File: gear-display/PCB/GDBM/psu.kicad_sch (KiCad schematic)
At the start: 10 parts

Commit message: new features
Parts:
- added C? (x2): C_1206_10u_50V, KD_Capacitor:C_1206_3216Metric, symbol KD_Capacitor:C_1206_10u_50V
- added C?: C_0603_100n_X7R_100V, KD_Capacitor:C_0603_1608Metric, symbol KD_Capacitor:C_0603_100n_X7R_100V
- added U?: DC_DC_5V_0A5_K78U05-500R3, KD_IC_DCDC_Converter:DC_DC_Mornsun_K78U05-500R3_H, symbol KD_IC_Regulator_DC_Converter:DC_DC_5V_0A5_K78U05-500R3
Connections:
- net +12V: now also U?.1 (VI)
- net GND: now also C?.2, C?.2, C?.2, U?.2 (GND)
- new net +5V: C?.1, C?.1, C?.1, U?.3 (VO)
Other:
- moved on the sheet: C?, D?, F?, J?, U?

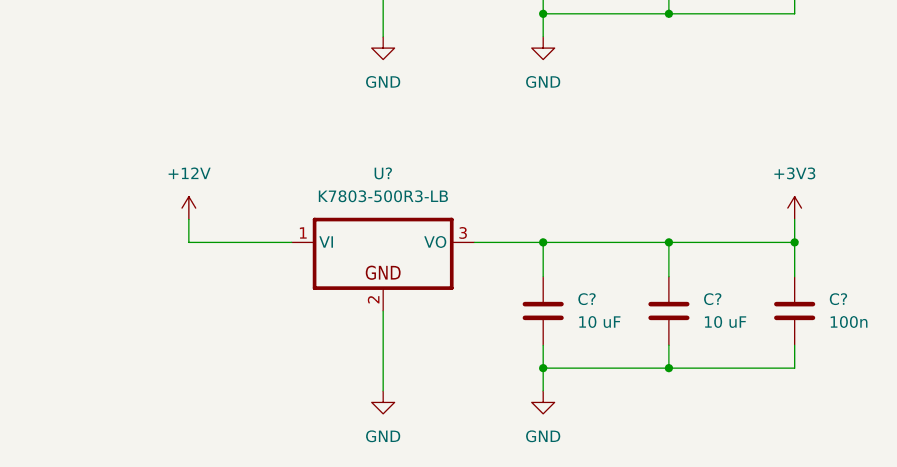
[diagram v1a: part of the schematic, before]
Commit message: changed to match simhub conf
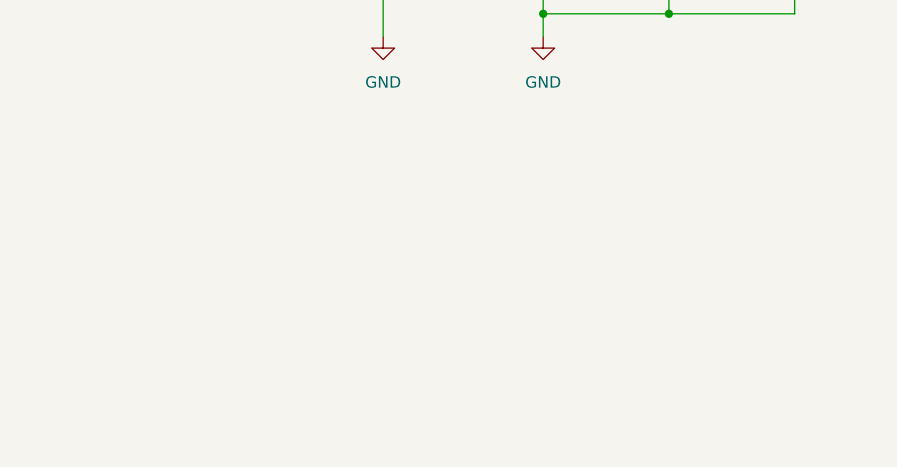
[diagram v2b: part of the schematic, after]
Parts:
- removed C?: C_0603_100n_X7R_100V, KD_Capacitor:C_0603_1608Metric, symbol KD_Capacitor:C_0603_100n_X7R_100V
- removed C? (x2): C_1206_10u_50V, KD_Capacitor:C_1206_3216Metric, symbol KD_Capacitor:C_1206_10u_50V
- removed U?: DC_DC_3V3+-_0A5_K7803-500R3-LB, KD_IC_DCDC_Converter:DC_DC_Mornsun_K78xx-500R3-LB, symbol KD_IC_Regulator_DC_Converter:DC_DC_3V3+-_0A5_K7803-500R3-LB

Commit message: rikki
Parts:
- removed D?: TVS_36V_SMAJ36CA, KD_Diode:D_SMA, symbol KD_Diode:TVS_36V_SMAJ36CA
- added D2: TVS_12V_LF_SMAJ12CA, KD_Diode:DIOC530X280X230_SMA_A, symbol KD_Diode:TVS_12V_LF_SMAJ12CA
- F1: renamed from F?; footprint KD_Resistor:R_1206_3216Metric -> KD_Resistor:RESC3216X70N
- gave numbers to parts that had none: 8
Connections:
- net +12V: now also D2.1 (K)
- net GND renamed Earth
- net Earth: now also D2.2 (A)
- no-connect marks 0 -> 1
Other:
- note removed: "SMAJ16 or something?"

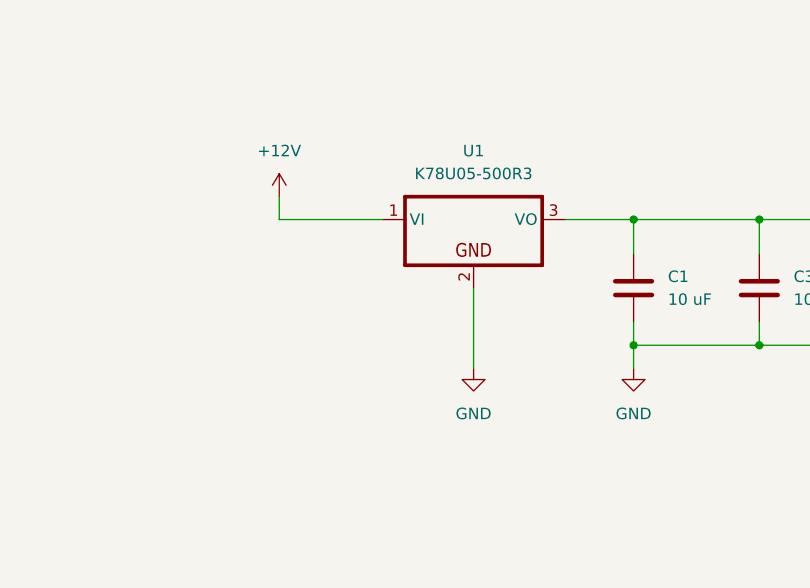
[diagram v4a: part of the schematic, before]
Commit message: PSU and LED powering changed
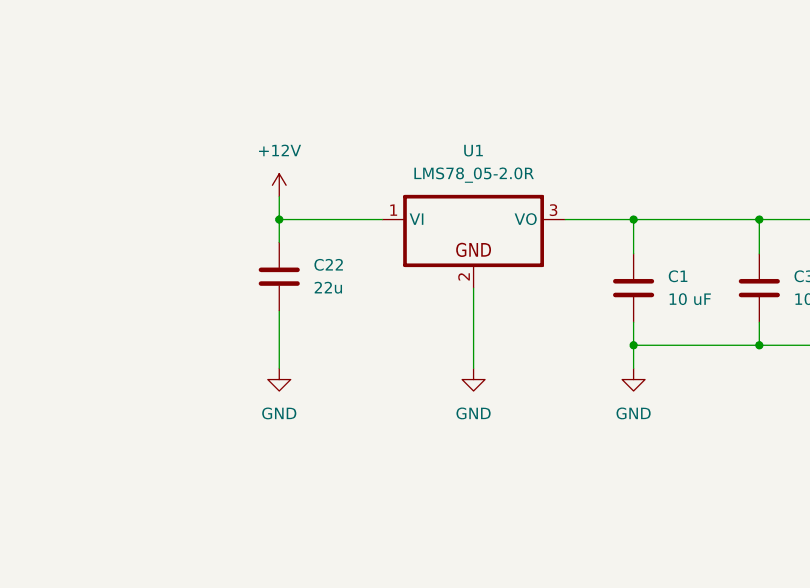
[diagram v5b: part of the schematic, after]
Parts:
- added C22: C_0805_22u_X5R_10V, KD_Capacitor:CAPC2012X135N, symbol KD_Capacitor:C_0805_22u_X5R_10V
- C1, C2, C3: footprint KD_Capacitor:C_1206_3216Metric -> KD_Capacitor:CAPC3216X150N
- C4, C5: footprint KD_Capacitor:C_0603_1608Metric -> KD_Capacitor:CAPC1608X90N
- U1: footprint KD_IC_DCDC_Converter:DC_DC_Mornsun_K78U05-500R3_H -> KD_IC_DCDC_Converter:DC_DC_GAPTEC_OKI-78SR-5_H; symbol KD_IC_Regulator_DC_Converter:DC_DC_5V_0A5_K78U05-500R3 -> KD_IC_Regulator_DC_Converter:DC_DC_5V_2A0_GAPTEC_OKI-78SR-5_H; Code K78U05-500R3 -> LMS78_05-2.0R; MFG_PartNo K78U05-500R3 -> LMS78_05-2.0R; Manufacturer Mornsun America, LLC -> GAPTEC Electronic; Price 3 -> 5; Supplier_PartNo 2725-K78U05-500R3-ND -> 3182-LMS78_05-2.0R-ND
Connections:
- net +12V: now also C22.1
- net Earth: now also C22.2
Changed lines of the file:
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@@
   (junction (at 181.61 111.76) (diameter 0) (color 0 0 0 0)
+  )
+  (junction (at 128.27 97.79) (diameter 0) (color 0 0 0 0)
   )
   (junction (at 167.64 97.79) (diameter 0) (color 0 0 0 0)
@@
     (stroke (width 0) (type default) (color 0 0 0 0))
   )
+  (wire (pts (xy 128.27 114.3) (xy 128.27 107.95))
+    (stroke (width 0) (type default) (color 0 0 0 0))
+  )
   (wire (pts (xy 104.14 149.86) (xy 104.14 147.32))
     (stroke (width 0) (type default) (color 0 0 0 0))
@@
     (stroke (width 0) (type default) (color 0 0 0 0))
   )
+  (wire (pts (xy 128.27 97.79) (xy 128.27 100.33))
+    (stroke (width 0) (type default) (color 0 0 0 0))
+  )
   (wire (pts (xy 181.61 109.22) (xy 181.61 111.76))
     (stroke (width 0) (type default) (color 0 0 0 0))
@@
       (effects (font (size 1.27 1.27)) (justify left) hide)
     )
-    (property "Footprint" "KD_Capacitor:C_0603_1608Metric" (id 2) (at 182.88 40.64 0)
+    (property "Footprint" "KD_Capacitor:CAPC1608X90N" (id 2) (at 182.88 40.64 0)
       (effects (font (size 1.27 1.27)) (justify left) hide)
     )
@@
     (pin "2")
   )
-  (symbol (lib_id "KD_IC_Regulator_DC_Converter:DC_DC_5V_0A5_K78U05-500R3") (at 149.86 97.79 0) (unit 1)
+  (symbol (lib_id "KD_IC_Regulator_DC_Converter:DC_DC_5V_2A0_GAPTEC_OKI-78SR-5_H") (at 149.86 97.79 0) (unit 1)
     (in_bom yes) (on_board yes) (fields_autoplaced)
     (property "Reference" "U1" (id 0) (at 149.86 90.17 0))
@@
       (effects (font (size 1.27 1.27)) (justify left) hide)
     )
-    (property "Footprint" "KD_IC_DCDC_Converter:DC_DC_Mornsun_K78U05-500R3_H" (id 2) (at 137.16 83.82 0)
-      (effects (font (size 1.27 1.27)) (justify left) hide)
-    )
-    (property "Datasheet" "https://www.mornsun-power.com/html/pdf/K78U05-500R3.html" (id 3) (at 137.16 86.36 0)
-      (effects (font (size 1.27 1.27)) (justify left) hide)
-    )
-    (property "Code" "K78U05-500R3" (id 4) (at 149.86 92.71 0))
-    (property "Manufacturer" "Mornsun America, LLC" (id 5) (at 137.16 68.58 0)
-      (effects (font (size 1.27 1.27)) (justify left) hide)
-    )
-    (property "MFG_PartNo" "K78U05-500R3" (id 6) (at 137.16 71.12 0)
+    (property "Footprint" "KD_IC_DCDC_Converter:DC_DC_GAPTEC_OKI-78SR-5_H" (id 2) (at 137.16 83.82 0)
+      (effects (font (size 1.27 1.27)) (justify left) hide)
+    )
+    (property "Datasheet" "https://gaptec-electronic.com/datenblaetter/LMS78_2.0R.pdf" (id 3) (at 137.16 86.36 0)
+      (effects (font (size 1.27 1.27)) (justify left) hide)
+    )
+    (property "Code" "LMS78_05-2.0R" (id 4) (at 149.86 92.71 0))
+    (property "Manufacturer" "GAPTEC Electronic" (id 5) (at 137.16 68.58 0)
+      (effects (font (size 1.27 1.27)) (justify left) hide)
+    )
+    (property "MFG_PartNo" "LMS78_05-2.0R" (id 6) (at 137.16 71.12 0)
       (effects (font (size 1.27 1.27)) (justify left) hide)
     )
@@
       (effects (font (size 1.27 1.27)) (justify left) hide)
     )
-    (property "Supplier_PartNo" "2725-K78U05-500R3-ND" (id 8) (at 137.16 76.2 0)
+    (property "Supplier_PartNo" "3182-LMS78_05-2.0R-ND" (id 8) (at 137.16 76.2 0)
       (effects (font (size 1.27 1.27)) (justify left) hide)
     )
@@
       (effects (font (size 1.27 1.27)) (justify left) hide)
     )
-    (property "Price" "3" (id 10) (at 137.16 81.28 0)
+    (property "Price" "5" (id 10) (at 137.16 81.28 0)
       (effects (font (size 1.27 1.27)) (justify left) hide)
     )
@@
     (pin "3")
   )
-  (symbol (lib_id "KD_Capacitor:C_1206_10u_50V") (at 167.64 105.41 0) (unit 1)
+  (symbol (lib_name "C_1206_10u_50V_1") (lib_id "KD_Capacitor:C_1206_10u_50V") (at 167.64 105.41 0) (unit 1)
     (in_bom yes) (on_board yes) (fields_autoplaced)
     (property "Reference" "C1" (id 0) (at 171.45 104.1399 0)
@@
       (effects (font (size 1.27 1.27)) (justify left) hide)
     )
-    (property "Footprint" "KD_Capacitor:C_1206_3216Metric" (id 2) (at 154.94 91.44 0)
+    (property "Footprint" "KD_Capacitor:CAPC3216X150N" (id 2) (at 154.94 91.44 0)
       (effects (font (size 1.27 1.27)) (justify left) hide)
     )
@@
       (effects (font (size 1.27 1.27)) (justify left) hide)
     )
-    (property "Footprint" "KD_Capacitor:C_1206_3216Metric" (id 2) (at 165.1 40.64 0)
+    (property "Footprint" "KD_Capacitor:CAPC3216X150N" (id 2) (at 165.1 40.64 0)
       (effects (font (size 1.27 1.27)) (justify left) hide)
     )
@@
     (pin "1")
   )
-  (symbol (lib_id "KD_Capacitor:C_0603_100n_X7R_100V") (at 195.58 105.41 0) (unit 1)
+  (symbol (lib_name "C_0603_100n_X7R_100V_1") (lib_id "KD_Capacitor:C_0603_100n_X7R_100V") (at 195.58 105.41 0) (unit 1)
     (in_bom yes) (on_board yes) (fields_autoplaced)
     (property "Reference" "C5" (id 0) (at 199.39 104.1399 0)
@@
       (effects (font (size 1.27 1.27)) (justify left) hide)
     )
-    (property "Footprint" "KD_Capacitor:C_0603_1608Metric" (id 2) (at 182.88 91.44 0)
+    (property "Footprint" "KD_Capacitor:CAPC1608X90N" (id 2) (at 182.88 91.44 0)
       (effects (font (size 1.27 1.27)) (justify left) hide)
     )
@@
     (pin "1")
     (pin "2")
+  )
+  (symbol (lib_id "power:GND") (at 128.27 114.3 0) (unit 1)
+    (in_bom yes) (on_board yes) (fields_autoplaced)
+    (property "Reference" "#PWR0145" (id 0) (at 128.27 120.65 0)
+      (effects (font (size 1.27 1.27)) hide)
+    )
+    (property "Value" "GND" (id 1) (at 128.27 119.38 0))
+    (property "Footprint" "" (id 2) (at 128.27 114.3 0)
+      (effects (font (size 1.27 1.27)) hide)
+    )
+    (property "Datasheet" "" (id 3) (at 128.27 114.3 0)
+      (effects (font (size 1.27 1.27)) hide)
+    )
+    (pin "1")
   )
   (symbol (lib_id "KD_Diode:Schottky_30V_1A_Toshiba_CUS10S30") (at 134.62 48.26 180) (unit 1)
@@
     (pin "2")
   )
-  (symbol (lib_id "KD_Capacitor:C_1206_10u_50V") (at 181.61 105.41 0) (unit 1)
+  (symbol (lib_name "C_1206_10u_50V_2") (lib_id "KD_Capacitor:C_1206_10u_50V") (at 181.61 105.41 0) (unit 1)
     (in_bom yes) (on_board yes) (fields_autoplaced)
     (property "Reference" "C3" (id 0) (at 185.42 104.1399 0)
@@
       (effects (font (size 1.27 1.27)) (justify left) hide)
     )
-    (property "Footprint" "KD_Capacitor:C_1206_3216Metric" (id 2) (at 168.91 91.44 0)
+    (property "Footprint" "KD_Capacitor:CAPC3216X150N" (id 2) (at 168.91 91.44 0)
       (effects (font (size 1.27 1.27)) (justify left) hide)
     )
@@
     (pin "4")
   )
+  (symbol (lib_id "KD_Capacitor:C_0805_22u_X5R_10V") (at 128.27 104.14 0) (unit 1)
+    (in_bom yes) (on_board yes) (fields_autoplaced)
+    (property "Reference" "C22" (id 0) (at 132.08 102.8699 0)
+      (effects (font (size 1.27 1.27)) (justify left))
+    )
+    (property "Value" "C_0805_22u_X5R_10V" (id 1) (at 115.57 72.39 0)
+      (effects (font (size 1.27 1.27)) (justify left) hide)
+    )
+    (property "Footprint" "KD_Capacitor:CAPC2012X135N" (id 2) (at 115.57 90.17 0)
+      (effects (font (size 1.27 1.27)) (justify left) hide)
+    )
+    (property "Datasheet" "https://www.samsungsem.com/kr/support/product-search/mlcc/CL21A226MPQNNNE.jsp" (id 3) (at 115.57 92.71 0)
+      (effects (font (size 1.27 1.27)) (justify left) hide)
+    )
+    (property "Code" "22u" (id 4) (at 132.08 105.4099 0)
+      (effects (font (size 1.27 1.27)) (justify left))
+    )
+    (property "Manufacturer" "Samsung Electro-Mechanics" (id 5) (at 115.57 74.93 0)
+      (effects (font (size 1.27 1.27)) (justify left) hide)
+    )
+    (property "MFG_PartNo" "CL21A226MPQNNNE" (id 6) (at 115.57 77.47 0)
+      (effects (font (size 1.27 1.27)) (justify left) hide)
+    )
+    (property "Supplier" "Digi-Key" (id 7) (at 115.57 80.01 0)
+      (effects (font (size 1.27 1.27)) (justify left) hide)
+    )
+    (property "Supplier_PartNo" "1276-2910-1-ND" (id 8) (at 115.57 82.55 0)
+      (effects (font (size 1.27 1.27)) (justify left) hide)
+    )
+    (property "DNP" "F" (id 9) (at 115.57 85.09 0)
+      (effects (font (size 1.27 1.27)) (justify left) hide)
+    )
+    (property "Price" "0.15" (id 10) (at 115.57 87.63 0)
+      (effects (font (size 1.27 1.27)) (justify left) hide)
+    )
+    (pin "1")
+    (pin "2")
+  )
   (symbol (lib_id "power:GND") (at 195.58 64.77 0) (unit 1)

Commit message: fixes
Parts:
- U1: value DC_DC_5V_0A5_K78U05-500R3 -> DC_DC_5V_2A0_GAPTEC_OKI-78SR-5_H
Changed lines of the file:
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@@
     (in_bom yes) (on_board yes) (fields_autoplaced)
     (property "Reference" "U1" (id 0) (at 149.86 90.17 0))
-    (property "Value" "DC_DC_5V_0A5_K78U05-500R3" (id 1) (at 137.16 66.04 0)
+    (property "Value" "DC_DC_5V_2A0_GAPTEC_OKI-78SR-5_H" (id 1) (at 137.16 66.04 0)
       (effects (font (size 1.27 1.27)) (justify left) hide)
     )
